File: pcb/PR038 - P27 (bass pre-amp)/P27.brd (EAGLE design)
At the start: 45.1 x 52.1 mm, 52 parts, among them IC1 NE5532U, IC2 LM317, IC3 LM337, T1 BC549

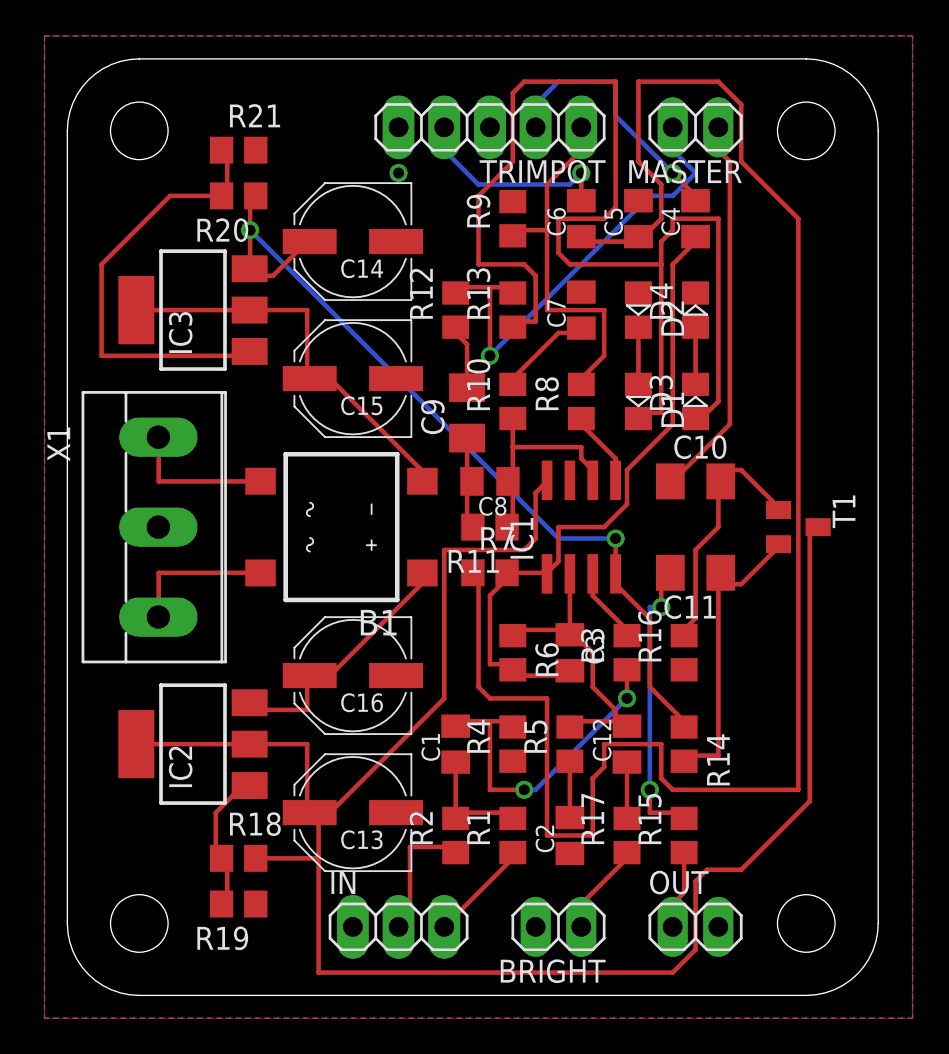
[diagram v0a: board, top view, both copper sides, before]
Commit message: 
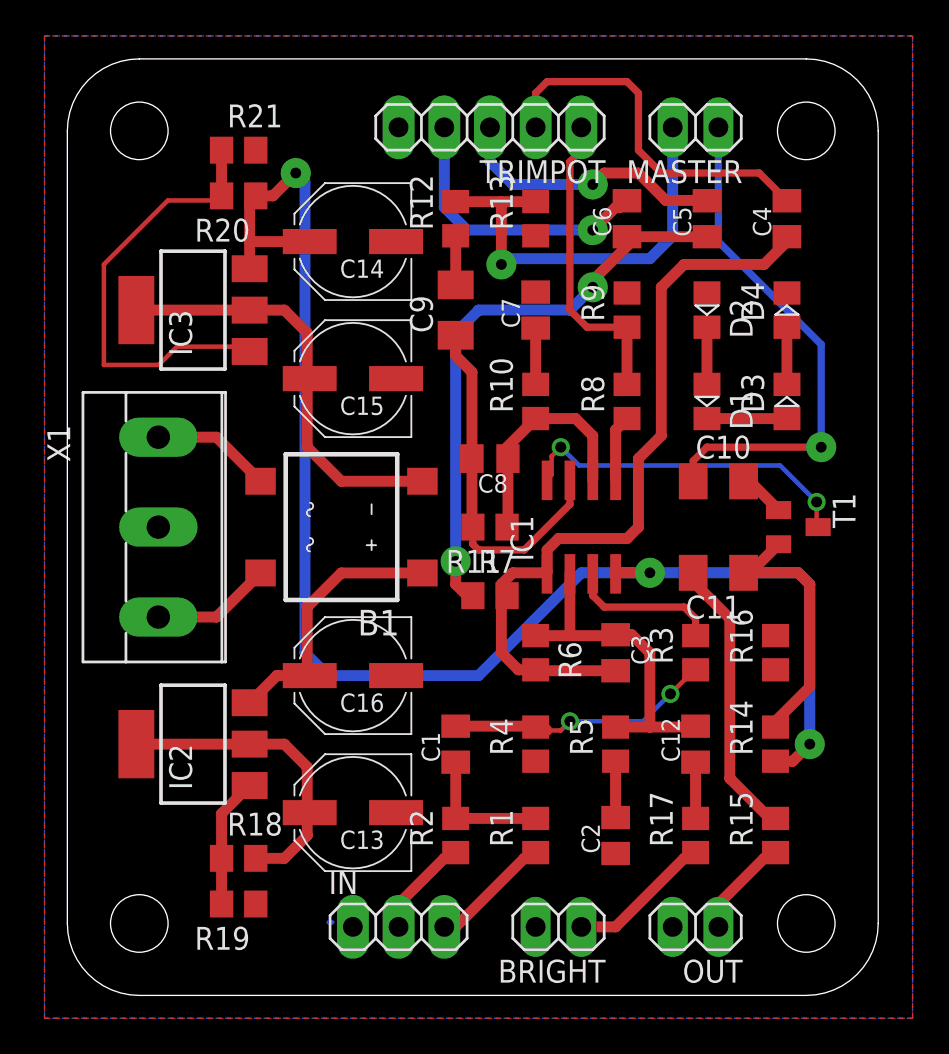
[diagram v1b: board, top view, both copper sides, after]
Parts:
- moved R9 8.13 mm to (31.1, 38.1)
- moved C9 5.75 mm to (21.6, 38.1)
- moved R13 5.24 mm to (26.0, 43.2)
- moved C4 5.08 mm to (40.0, 43.2)
- moved D3 5.08 mm to (40.0, 33.0)
- moved D4 5.08 mm to (40.0, 38.1)
- moved R12 5.08 mm to (21.6, 43.2)
- moved R14 5.08 mm to (39.4, 14.0), turned to 90 degrees
- moved R15 5.08 mm to (39.4, 8.89)
- moved R16 5.08 mm to (39.4, 19.1)
- moved C5 3.81 mm to (35.6, 43.2)
- moved D1 3.81 mm to (35.6, 33.0)
- moved D2 3.81 mm to (35.6, 38.1)
- moved C12 3.81 mm to (34.9, 14.0)
- moved R17 3.81 mm to (34.9, 8.89)
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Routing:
- net +12V: track 103.3 -> 36.9 mm, vias 0 -> 2
- net N$8: track 98.5 -> 32.6 mm, vias 0 -> 2
- net N$24: track 69.6 -> 4.83 mm
- net -12V: track 48.3 -> 81.8 mm, vias 2 -> 3
- net N$9: track 0.00 -> 15.4 mm, vias 0 -> 1
- net N$18: track 5.54 -> 19.9 mm
- net N$11: track 14.3 -> 2.60 mm
- net N$27: track 21.4 -> 28.7 mm, vias 0 -> 1
- net N$10: track 14.7 -> 20.7 mm, vias 1 -> 0
- net N$6: track 36.9 -> 42.9 mm
- net N$7: track 11.5 -> 15.9 mm
- net N$2: track 4.22 -> 8.41 mm
- net N$13: track 21.0 -> 17.2 mm
- net N$3: track 18.9 -> 15.1 mm
- net N$30: track 5.18 -> 8.06 mm
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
